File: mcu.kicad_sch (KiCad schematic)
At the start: 0 parts

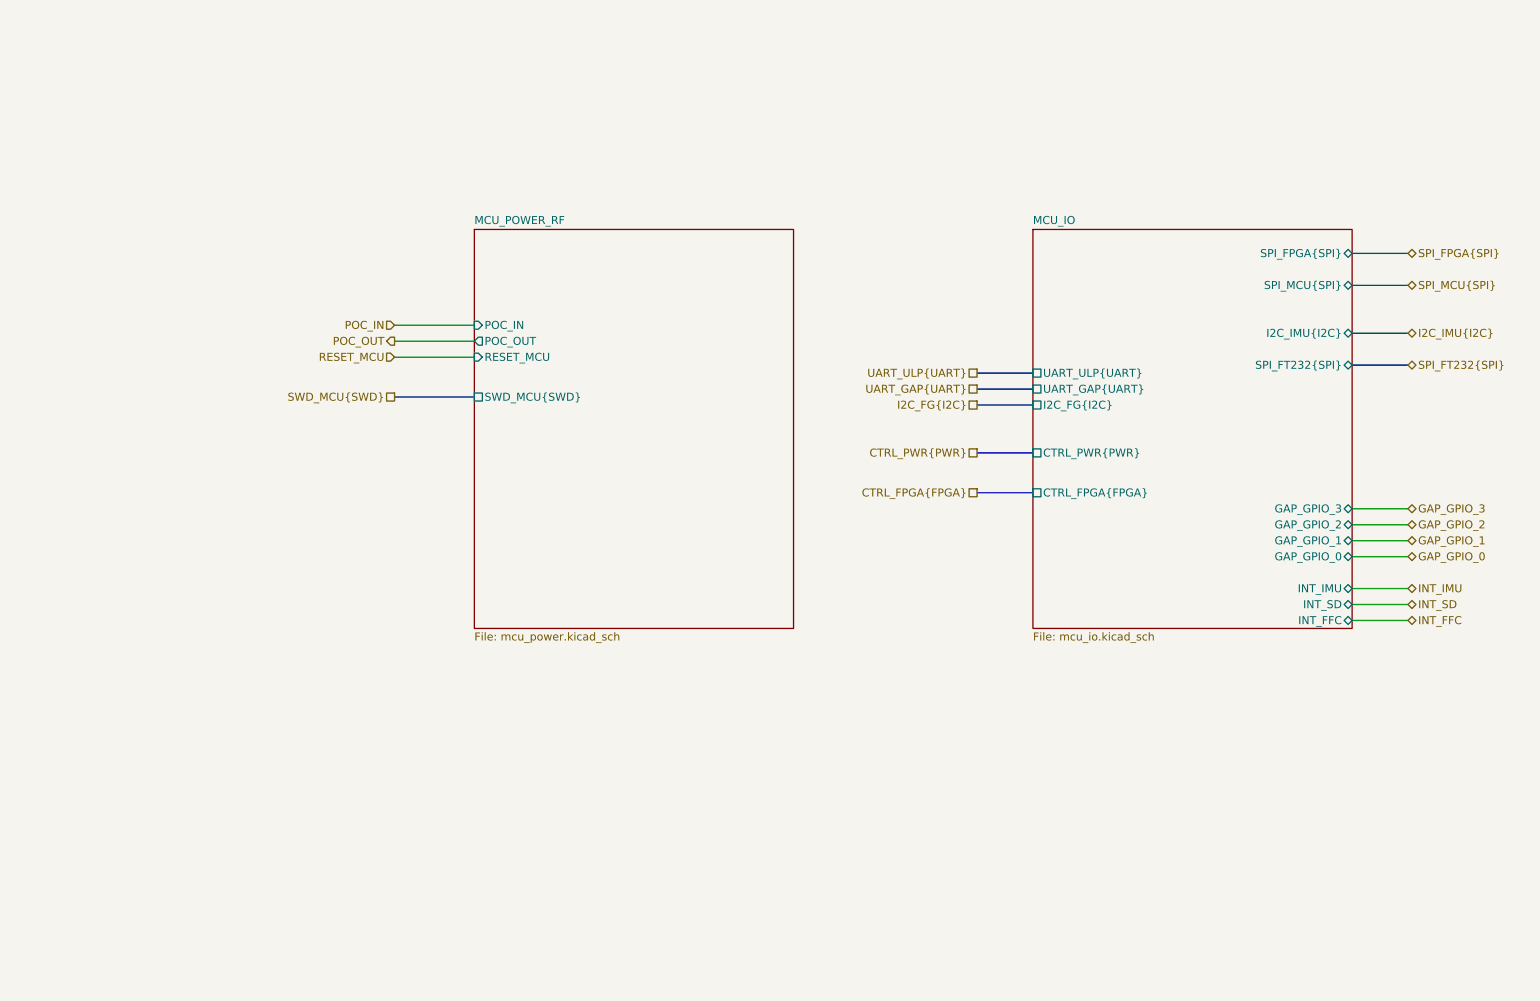
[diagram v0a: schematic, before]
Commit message: insert of gpio expander
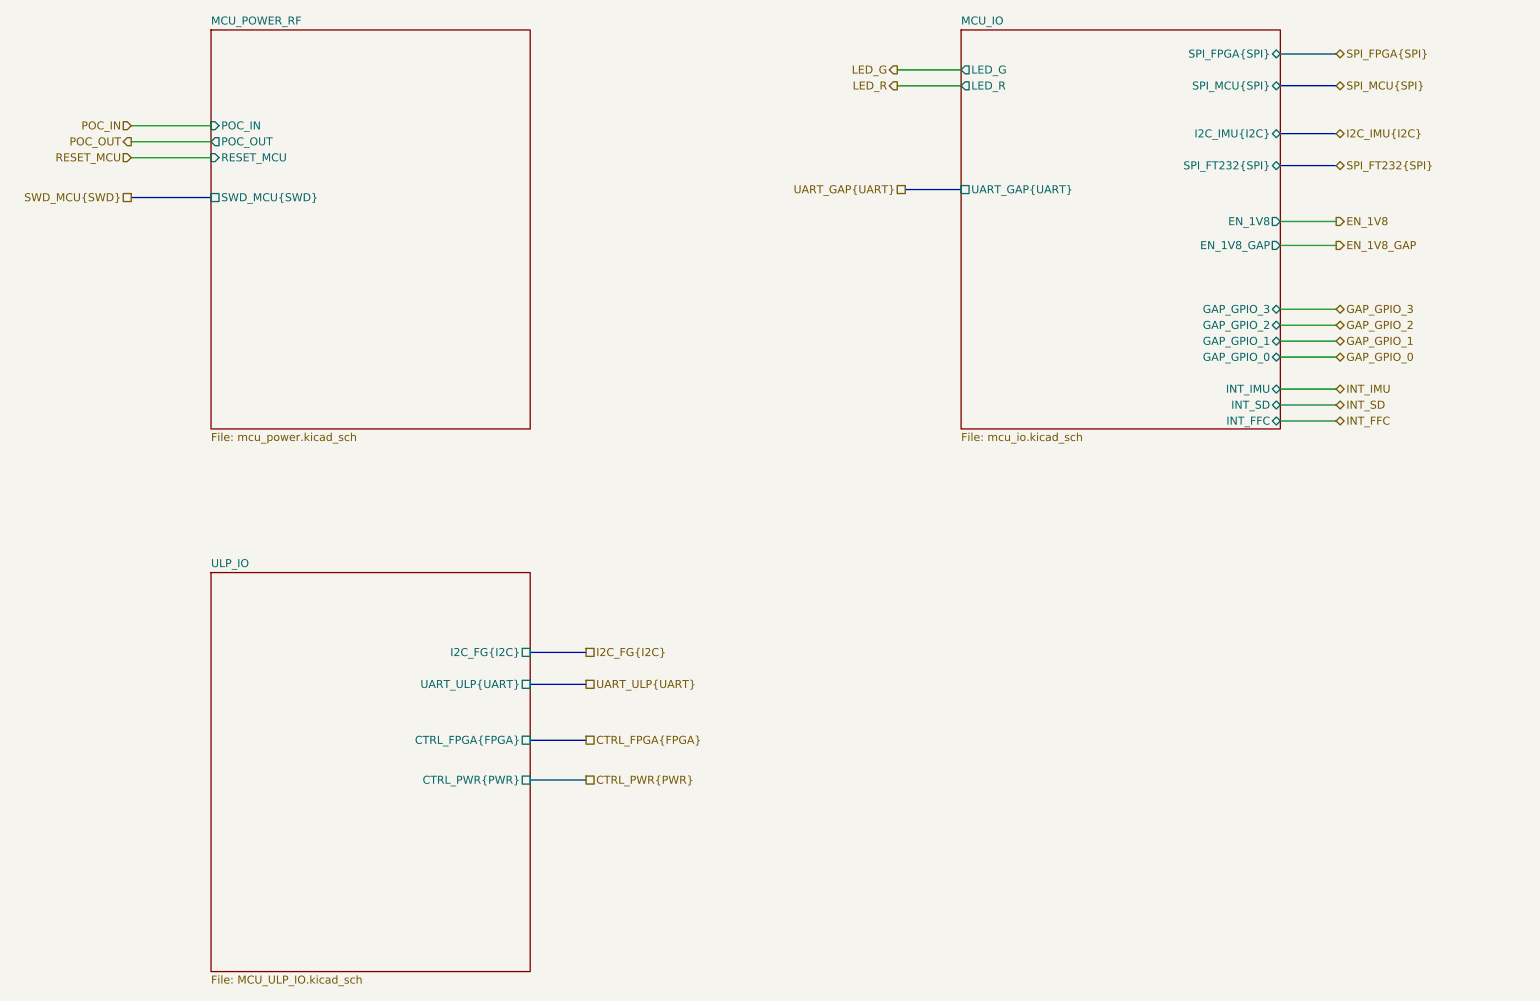
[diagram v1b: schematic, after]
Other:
- added sheet ULP_IO (MCU_ULP_IO.kicad_sch)
- sheet MCU_IO ports: added EN_1V8, EN_1V8_GAP, LED_G, LED_R; removed CTRL_FPGA{FPGA}, CTRL_PWR{PWR}, I2C_FG{I2C}, UART_ULP{UART}

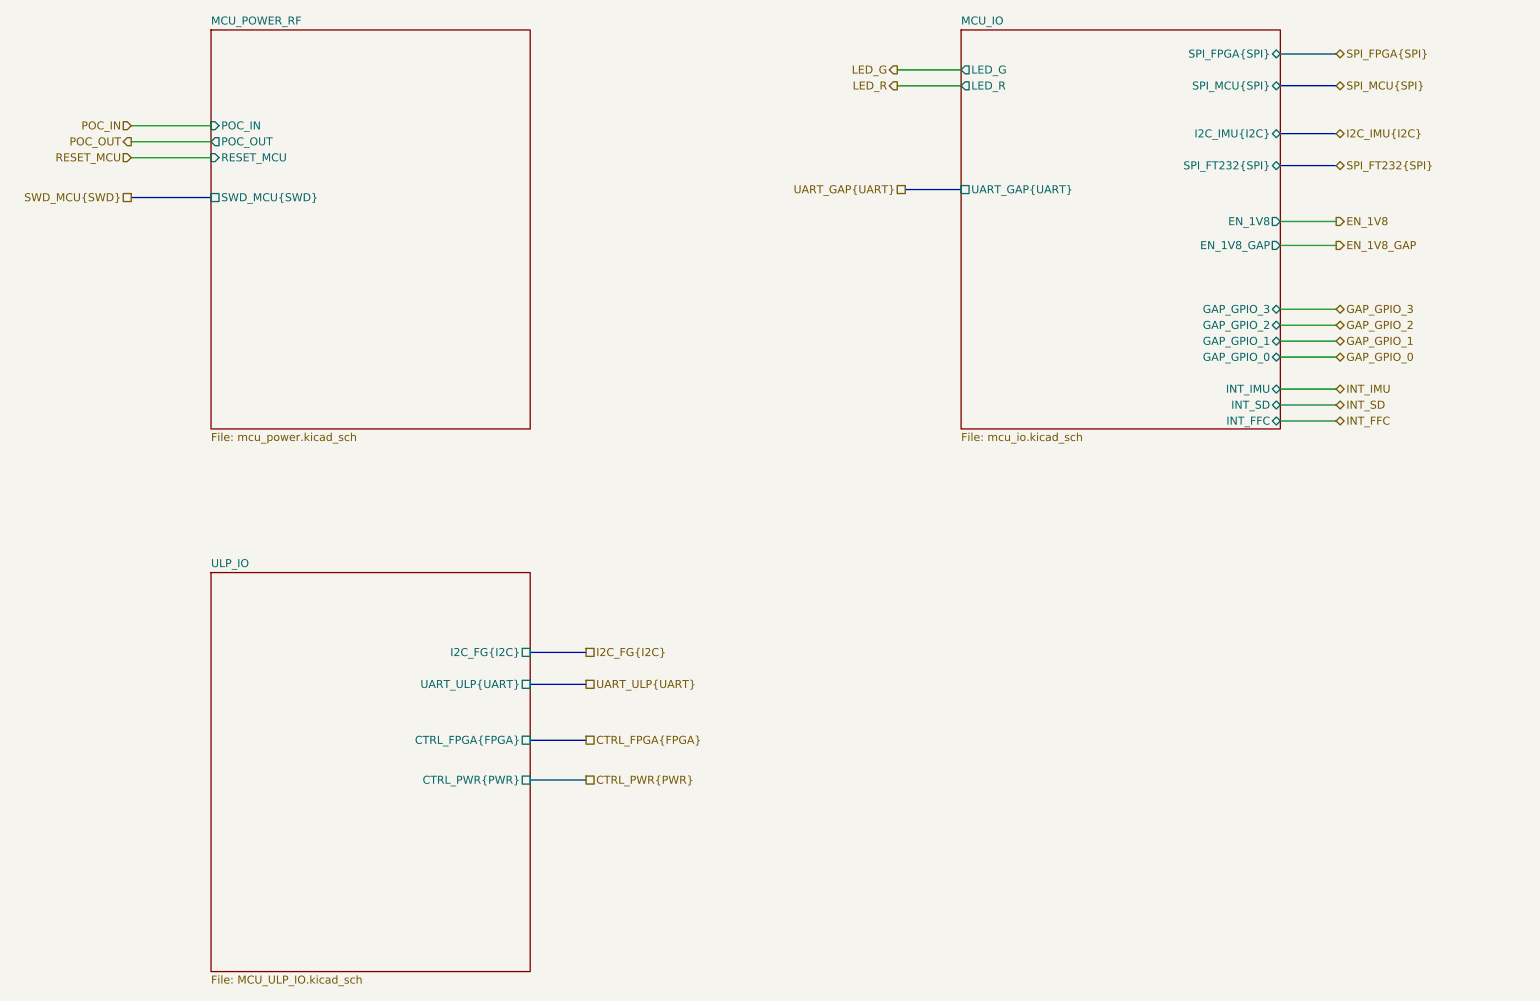
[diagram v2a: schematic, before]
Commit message: changes after first review: add lvl shifters, board at 1v8, new power tree
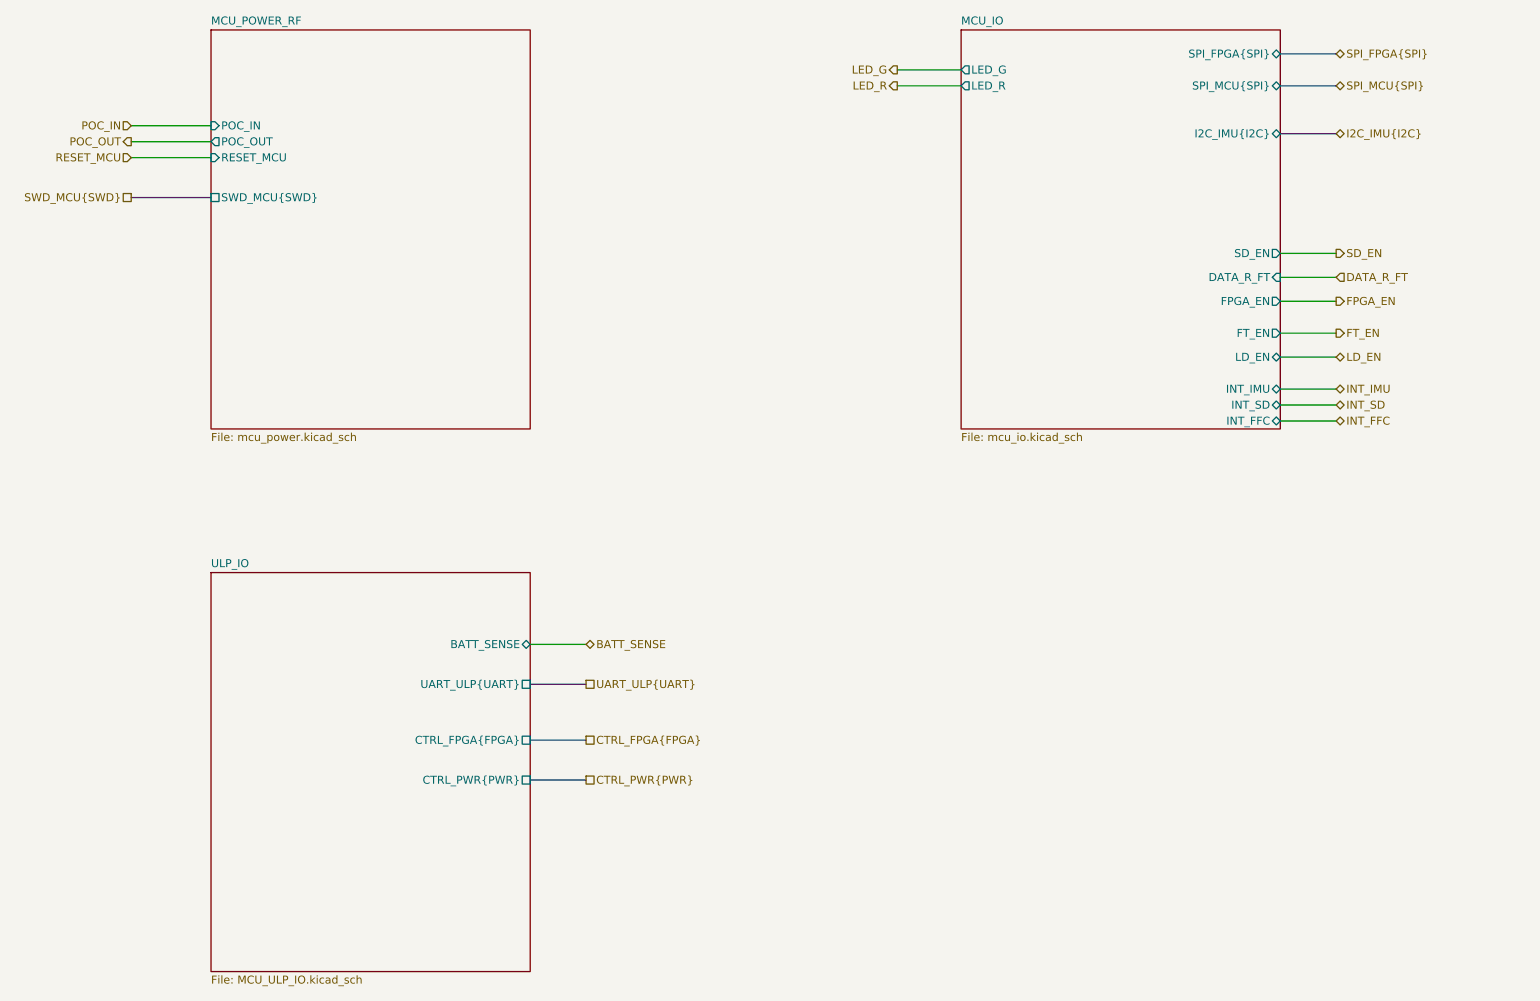
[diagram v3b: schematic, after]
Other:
- sheet MCU_IO ports: added DATA_R_FT, FPGA_EN, FT_EN, LD_EN, SD_EN; removed EN_1V8, EN_1V8_GAP, GAP_GPIO_0, GAP_GPIO_1, GAP_GPIO_2, GAP_GPIO_3, SPI_FT232{SPI}, UART_GAP{UART}
- sheet ULP_IO ports: added BATT_SENSE; removed I2C_FG{I2C}

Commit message: updated schematic and initial pcb placement
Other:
- sheet MCU_IO ports: added ULP_SSI{SPI}; removed LD_EN
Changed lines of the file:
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@@
-	(wire
-		(pts
-			(xy 214.63 81.28) (xy 223.52 81.28)
-		)
-		(stroke
-			(width 0)
-			(type default)
-		)
-	)
 	(wire
 		(pts
@@
 		(pts
 			(xy 214.63 38.1) (xy 223.52 38.1)
+		)
+		(stroke
+			(width 0)
+			(type default)
+		)
+	)
+	(bus
+		(pts
+			(xy 214.63 54.61) (xy 223.52 54.61)
 		)
 		(stroke
@@
 		)
 	)
+	(hierarchical_label "ULP_SSI{SPI}"
+		(shape bidirectional)
+		(at 223.52 54.61 0)
+		(effects
+			(font
+				(size 1.27 1.27)
+			)
+			(justify left)
+		)
+	)
 	(hierarchical_label "I2C_IMU{I2C}"
 		(shape bidirectional)
@@
 			)
 			(justify right)
-		)
-	)
-	(hierarchical_label "LD_EN"
-		(shape bidirectional)
-		(at 223.52 81.28 0)
-		(effects
-			(font
-				(size 1.27 1.27)
-			)
-			(justify left)
 		)
 	)
@@
 			)
 		)
-		(pin "LD_EN" bidirectional
-			(at 214.63 81.28 0)
-			(effects
-				(font
-					(size 1.27 1.27)
-				)
-				(justify right)
-			)
-		)
 		(pin "SD_EN" output
 			(at 214.63 64.77 0)
 			(effects
 				(font
+					(size 1.27 1.27)
+				)
+				(justify right)
+			)
+		)
+		(pin "ULP_SSI{SPI}" bidirectional
+			(at 214.63 54.61 0)
+			(effects
+				(font
